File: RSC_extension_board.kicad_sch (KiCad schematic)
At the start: 23 parts, among them J1 Conn_01x03, J2 Conn_01x03, J3 Conn_01x03, J4 Raspberry_Pi_4, J5 Conn_01x04, J6 USB_C_Receptacle_PowerOnly_6P, J7 Conn_01x02, Q1 BSS138, U1 USBLC6-2SC6

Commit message: some external power stuff
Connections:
- net +5V: now also D3.3, U1.5 (VBUS)
- net Earth: now also D3.1, D3.2, U1.2 (GND)
- net at R3.1: now also U1.4 (I/O2); no longer J6.B5 (CC2)
- net at R4.1: now also U1.6 (I/O1); no longer J6.A5 (CC1)
- net at U1.1 (I/O1): now also J6.A5 (CC1)
- net at U1.3 (I/O2): now also J6.B5 (CC2)
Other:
- note added: "right now power. maybe later battery things?"
- note removed: "battery things"
- moved on the sheet: D3, R3, R4, U1

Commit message: bit of power circuit
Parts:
- added C5: 100nF, Capacitor_SMD:C_0603_1608Metric_Pad1.08x0.95mm_HandSolder, symbol Device:C
- added F1: SMDC300F_24-2, SMDC300F_24-2:SMDC030F2, symbol SMDC300F_24-2:SMDC300F_24-2
- added SW1: SW_Wuerth_450301014042, Button_Switch_THT:SW_Slide-03_Wuerth-WS-SLTV_10x2.5x6.4_P2.54mm, symbol Switch:SW_Wuerth_450301014042
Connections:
- net +5V: now also C5.2, SW1.2 (C); no longer D3.3, J6.A9 (VBUS), J6.B9 (VBUS), U1.5 (VBUS)
- net Earth: now also C5.1
- new net: F1.2, SW1.1 (B)
- new net: D3.3, F1.1, J6.A9 (VBUS), J6.B9 (VBUS), U1.5 (VBUS)
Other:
- moved on the sheet: D3

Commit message: updated fuse
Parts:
- removed F1: SMDC300F_24-2, SMDC300F_24-2:SMDC030F2, symbol SMDC300F_24-2:SMDC300F_24-2
- added F?: PTSLR08058V350, FUSC2516X100N, symbol PTSLR08058V350:PTSLR08058V350
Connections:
- net at SW1.1 (B): now also F?.2
- net at D3.3, J6.A9 (VBUS), J6.B9 (VBUS)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: now also F?.1
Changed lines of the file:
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@@
-	)
-	(symbol
-		(lib_id "SMDC300F_24-2:SMDC300F_24-2")
-		(at 52.07 151.13 0)
-		(unit 1)
-		(exclude_from_sim no)
-		(in_bom yes)
-		(on_board yes)
-		(dnp no)
-		(fields_autoplaced yes)
-		(property "Reference" "F1"
-			(at 60.96 143.51 0)
-			(effects
-				(font
-					(size 1.27 1.27)
-				)
-			)
-		)
-		(property "Value" "SMDC300F_24-2"
-			(at 60.96 146.05 0)
-			(effects
-				(font
-					(size 1.27 1.27)
-				)
-			)
-		)
-		(property "Footprint" "SMDC300F_24-2:SMDC030F2"
-			(at 66.04 247.32 0)
-			(effects
-				(font
-					(size 1.27 1.27)
-				)
-				(justify left top)
-				(hide yes)
-			)
-		)
-		(property "Datasheet" "https://www.littelfuse.com/~/media/electronics/product_specifications/resettable_ptcs/littelfuse_ptc_smdc030f_2_product_specification.pdf.pdf"
-			(at 66.04 347.32 0)
-			(effects
-				(font
-					(size 1.27 1.27)
-				)
-				(justify left top)
-				(hide yes)
-			)
-		)
-		(property "Description" "Resettable Fuses - PPTC 24V    3A-HD  40A MAX"
-			(at 52.07 151.13 0)
-			(effects
-				(font
-					(size 1.27 1.27)
-				)
-				(hide yes)
-			)
-		)
-		(property "Height" "1"
-			(at 66.04 547.32 0)
-			(effects
-				(font
-					(size 1.27 1.27)
-				)
-				(justify left top)
-				(hide yes)
-			)
-		)
-		(property "Manufacturer_Name" "LITTELFUSE"
-			(at 66.04 647.32 0)
-			(effects
-				(font
-					(size 1.27 1.27)
-				)
-				(justify left top)
-				(hide yes)
-			)
-		)
-		(property "Manufacturer_Part_Number" "SMDC300F/24-2"
-			(at 66.04 747.32 0)
-			(effects
-				(font
-					(size 1.27 1.27)
-				)
-				(justify left top)
-				(hide yes)
-			)
-		)
-		(property "Mouser Part Number" "650-SMDC300F/24-2"
-			(at 66.04 847.32 0)
-			(effects
-				(font
-					(size 1.27 1.27)
-				)
-				(justify left top)
-				(hide yes)
-			)
-		)
-		(property "Mouser Price/Stock" "https://www.mouser.co.uk/ProductDetail/Littelfuse/SMDC300F-24-2?qs=pBN%2FbMTRZdcsk20bJLIO5A%3D%3D"
-			(at 66.04 947.32 0)
-			(effects
-				(font
-					(size 1.27 1.27)
-				)
-				(justify left top)
-				(hide yes)
-			)
-		)
-		(property "Arrow Part Number" "SMDC300F/24-2"
-			(at 66.04 1047.32 0)
-			(effects
-				(font
-					(size 1.27 1.27)
-				)
-				(justify left top)
-				(hide yes)
-			)
-		)
-		(property "Arrow Price/Stock" "https://www.arrow.com/en/products/smdc300f24-2/littelfuse?utm_currency=USD&region=nac"
-			(at 66.04 1147.32 0)
-			(effects
-				(font
-					(size 1.27 1.27)
-				)
-				(justify left top)
-				(hide yes)
-			)
-		)
-		(pin "2"
-		)
-		(pin "1"
-		)
-		(instances
-			(project ""
-				(path "/1f48ed4c-84ce-4e77-88fc-25bf92dcee2d"
-					(reference "F1")
-					(unit 1)
-				)
-			)
-		)
 	)
 	(symbol
@@
 					(unit 1)
 				)
+			)
+		)
+	)
+	(symbol
+		(lib_id "PTSLR08058V350:PTSLR08058V350")
+		(at 50.8 139.7 0)
+		(unit 1)
+		(exclude_from_sim no)
+		(in_bom yes)
+		(on_board yes)
+		(dnp no)
+		(fields_autoplaced yes)
+		(property "Reference" "F?"
+			(at 57.15 146.05 0)
+			(effects
+				(font
+					(size 1.27 1.27)
+				)
+				(justify left)
+			)
+		)
+		(property "Value" "PTSLR08058V350"
+			(at 57.15 148.082 0)
+			(effects
+				(font
+					(size 1.27 1.27)
+				)
+				(justify left)
+			)
+		)
+		(property "Footprint" "FUSC2516X100N"
+			(at 67.31 234.62 0)
+			(effects
+				(font
+					(size 1.27 1.27)
+				)
+				(justify left top)
+				(hide yes)
+			)
+		)
+		(property "Datasheet" "https://www.eaton.com/content/dam/eaton/products/electronic-components/resources/data-sheet/eaton-ptslr0805-surface-mount-resettable-fuse-data-sheet.pdf"
+			(at 67.31 334.62 0)
+			(effects
+				(font
+					(size 1.27 1.27)
+				)
+				(justify left top)
+				(hide yes)
+			)
+		)
+		(property "Description" "PTSLR 0805 3.5A"
+			(at 61.214 154.432 0)
+			(effects
+				(font
+					(size 1.27 1.27)
+				)
+				(hide yes)
+			)
+		)
+		(property "Height" "1"
+			(at 67.31 534.62 0)
+			(effects
+				(font
+					(size 1.27 1.27)
+				)
+				(justify left top)
+				(hide yes)
+			)
+		)
+		(property "Manufacturer_Name" "Eaton"
+			(at 67.31 634.62 0)
+			(effects
+				(font
+					(size 1.27 1.27)
+				)
+				(justify left top)
+				(hide yes)
+			)
+		)
+		(property "Manufacturer_Part_Number" "PTSLR08058V350"
+			(at 67.31 734.62 0)
+			(effects
+				(font
+					(size 1.27 1.27)
+				)
+				(justify left top)
+				(hide yes)
+			)
+		)
+		(property "Mouser Part Number" ""
+			(at 67.31 834.62 0)
+			(effects
+				(font
+					(size 1.27 1.27)
+				)
+				(justify left top)
+				(hide yes)
+			)
+		)
+		(property "Mouser Price/Stock" ""
+			(at 67.31 934.62 0)
+			(effects
+				(font
+					(size 1.27 1.27)
+				)
+				(justify left top)
+				(hide yes)
+			)
+		)
+		(property "Arrow Part Number" ""
+			(at 67.31 1034.62 0)
+			(effects
+				(font
+					(size 1.27 1.27)
+				)
+				(justify left top)
+				(hide yes)
+			)
+		)
+		(property "Arrow Price/Stock" ""
+			(at 67.31 1134.62 0)
+			(effects
+				(font
+					(size 1.27 1.27)
+				)
+				(justify left top)
+				(hide yes)
+			)
+		)
+		(pin "1"
+		)
+		(pin "2"
+		)
+		(instances
+			(project ""
+				(path "/1f48ed4c-84ce-4e77-88fc-25bf92dcee2d"
+					(reference "F?")
+					(unit 1)
+				)

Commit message: save
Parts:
- gave numbers to parts that had none: 1
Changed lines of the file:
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@@
 		(dnp no)
 		(fields_autoplaced yes)
-		(property "Reference" "F?"
+		(property "Reference" "F1"
 			(at 57.15 146.05 0)
 			(effects
@@
 			(project ""
 				(path "/1f48ed4c-84ce-4e77-88fc-25bf92dcee2d"
-					(reference "F?")
+					(reference "F1")
 					(unit 1)
 				)

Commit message: qwiic connector and 3.3v led out
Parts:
- added C7: 100nF, Capacitor_SMD:C_0603_1608Metric_Pad1.08x0.95mm_HandSolder, symbol Device:C
- added G1: qwiic_Logo, symbol SparkFun-Qwiic:qwiic_Logo
- added J8: Conn_01x03, Connector_PinHeader_2.54mm:PinHeader_1x03_P2.54mm_Horizontal, symbol Connector_Generic:Conn_01x03
- added J9: PRT-14417, PRT-14417:SPARKFUN_PRT-14417, symbol PRT-14417:PRT-14417
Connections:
- net +3.3V: now also C7.1, J8.1 (Pin_1), J9.2
- net Earth: now also C7.2, J8.3 (Pin_3), J9.1
- net LED_3.3V: now also J8.2 (Pin_2)
- net SDA: now reaches J4.3 (SDA_I2C1/GPIO02)
- net SDA: now also J9.3
- net SCL: now reaches J4.5 (SCL_I2C1/GPIO03)
- net SCL: now also J9.4

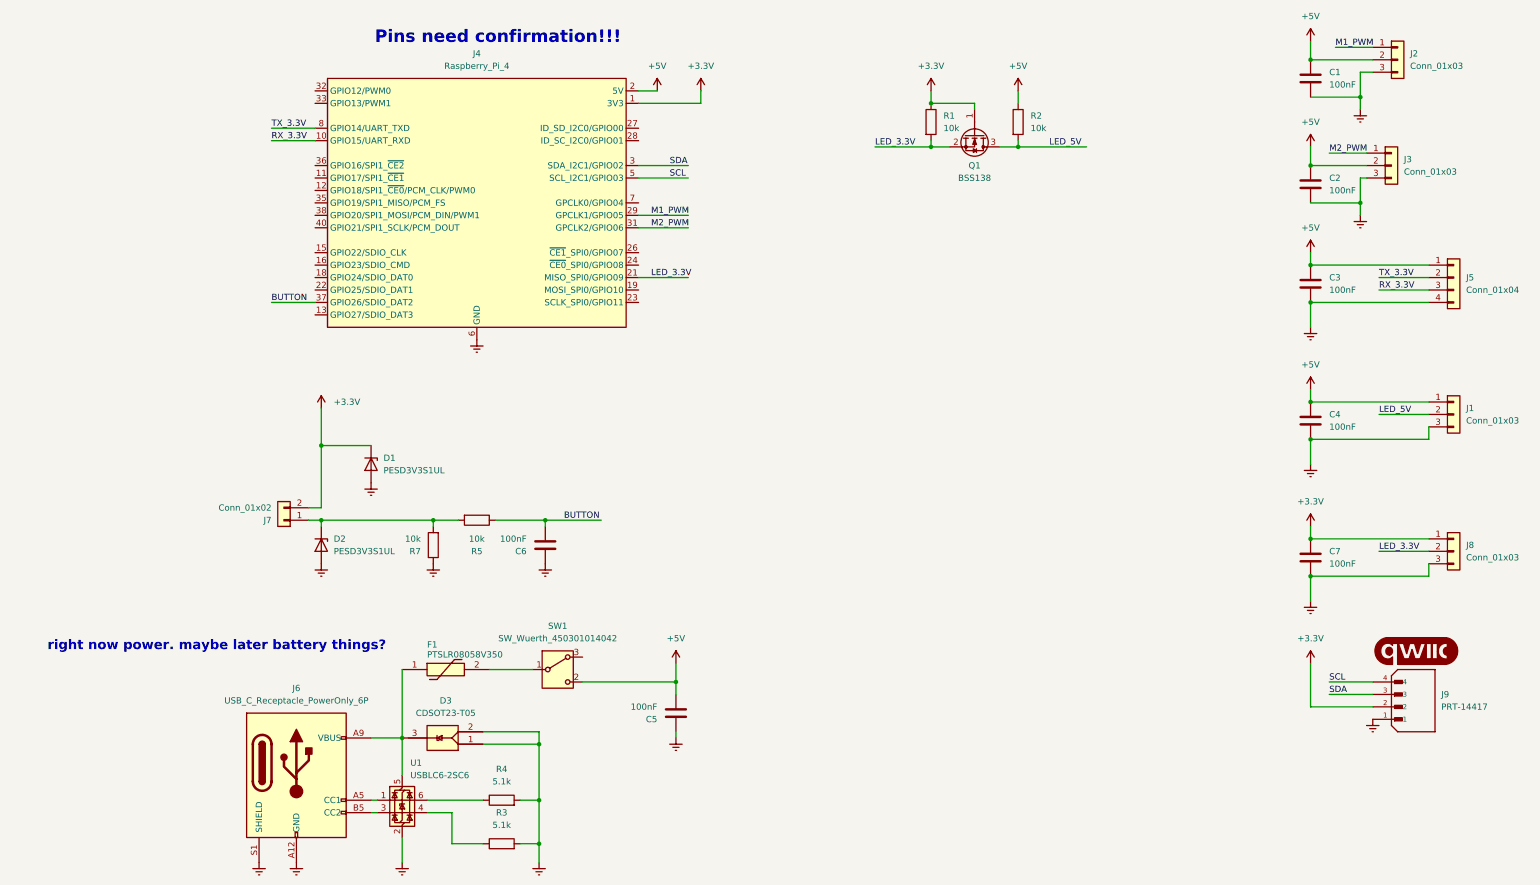
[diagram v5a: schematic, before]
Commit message: new tvs diodes
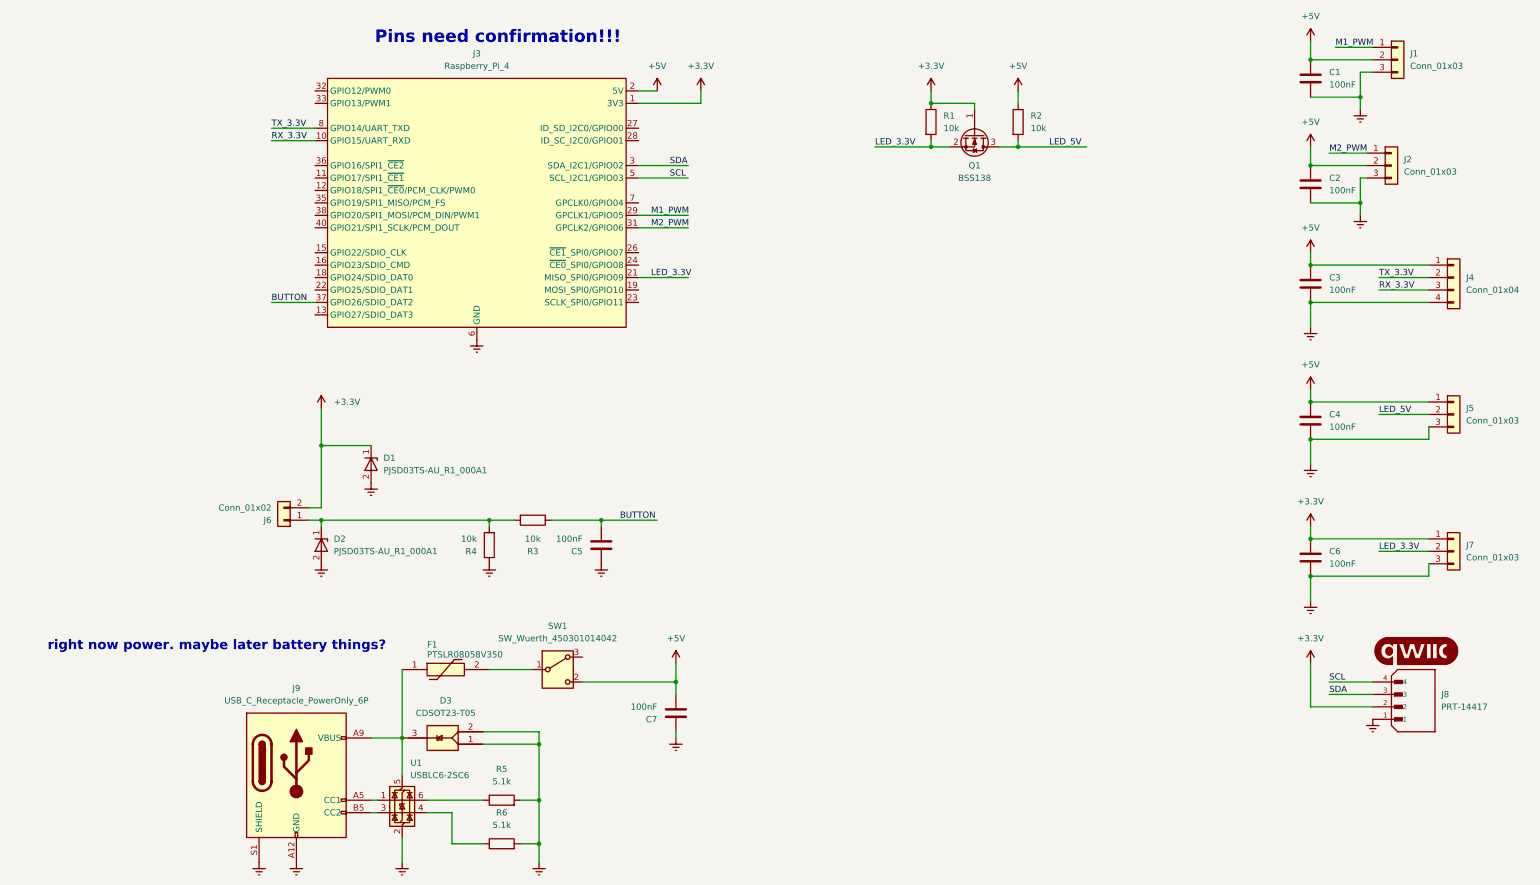
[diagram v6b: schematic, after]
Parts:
- removed D1, D2: PESD3V3S1UL, Diode_SMD:D_SOD-882, symbol Diode:PESD3V3S1UL
- added D1, D2: PJSD03TS-AU_R1_000A1, SODFL1608X65N, symbol PJSD03TS-AU_R1_000A1:PJSD03TS-AU_R1_000A1
- renumbered C6 to C5, C7 to C6, C5 to C7, J2 to J1, J3 to J2, J4 to J3, J5 to J4, J1 to J5, J7 to J6, J8 to J7, J9 to J8, J6 to J9, R5 to R3, R7 to R4, R4 to R5, R3 to R6
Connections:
- net +3.3V: now also D1.1 (K)
- net Earth: now also D1.2 (A), D2.2 (A)
- net at J6.1 (Pin_1), R3.2, R4.2: now also D2.1 (K)
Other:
- moved on the sheet: C5, R3, R4

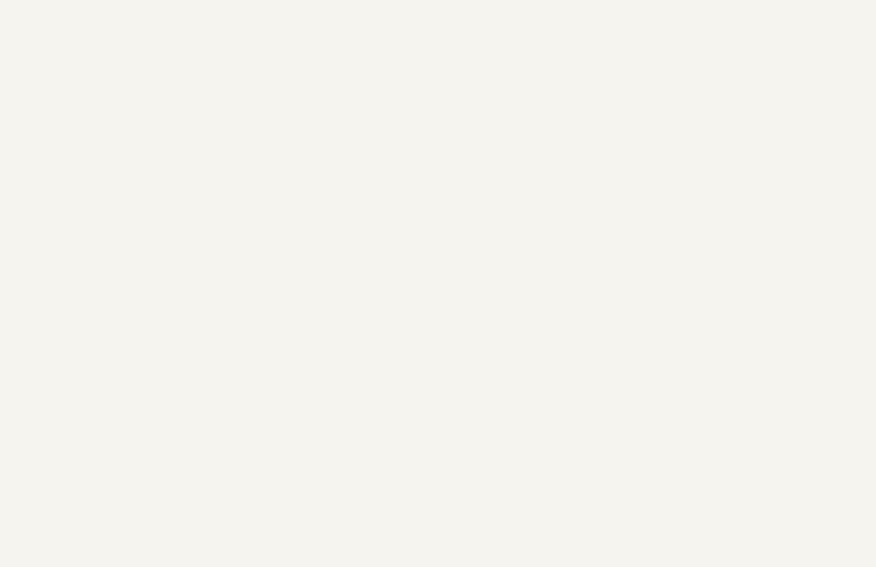
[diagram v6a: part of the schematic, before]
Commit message: added power LED
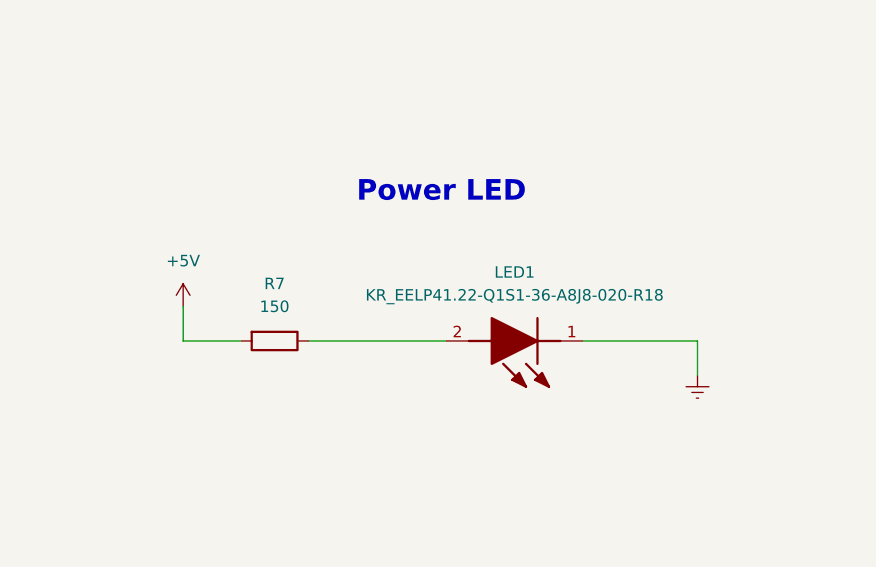
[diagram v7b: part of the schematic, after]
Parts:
- added LED1: KR_EELP41.22-Q1S1-36-A8J8-020-R18, KR_EELP41.22-Q1S1-36-A8J8-020-R18:KREELP4122Q1S136A8J8020R18, symbol KR_EELP41_22-Q1S1-36-A8J8-020-:KR_EELP41.22-Q1S1-36-A8J8-020-R18
- added R7: 150, Resistor_SMD:R_0603_1608Metric_Pad0.98x0.95mm_HandSolder, symbol Device:R
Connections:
- net +5V: now also R7.2
- net Earth: now also LED1.1 (K)
- new net: LED1.2 (A), R7.1
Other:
- note added: "Power LED"

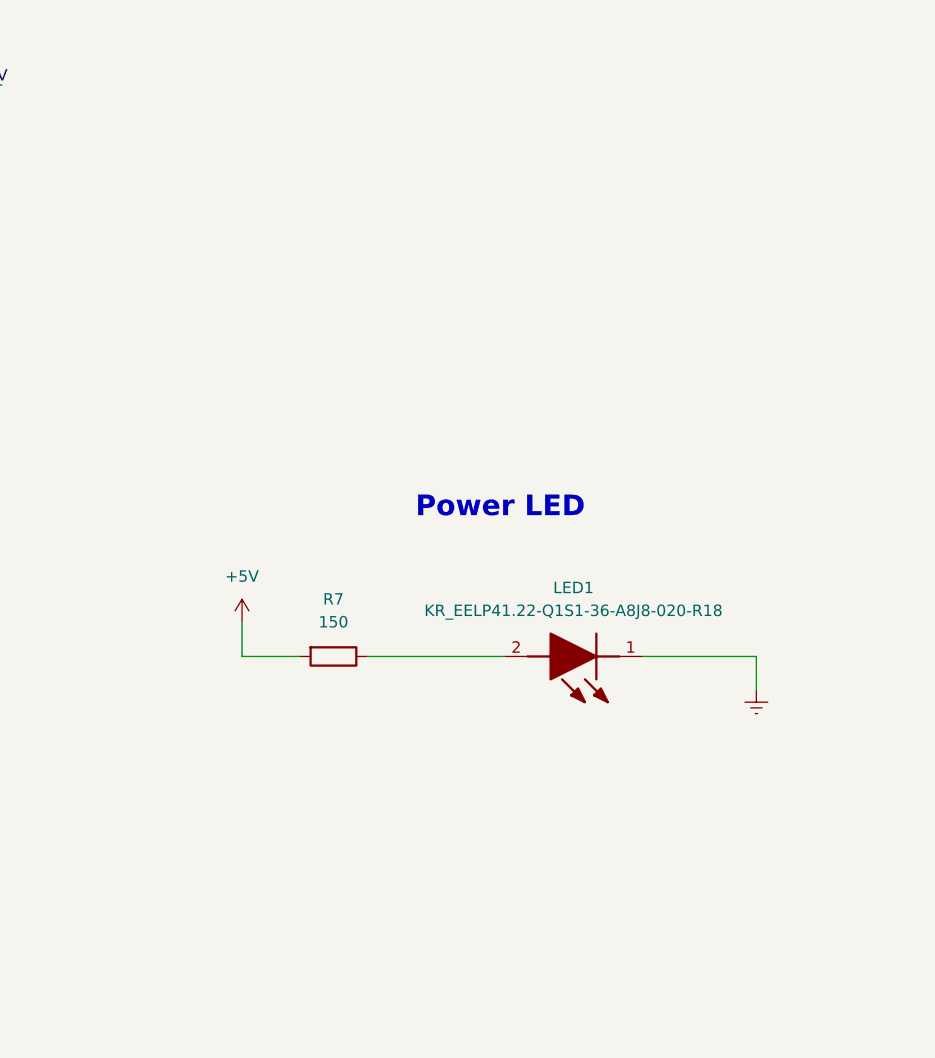
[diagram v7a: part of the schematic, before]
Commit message: added possibility for button led dimming
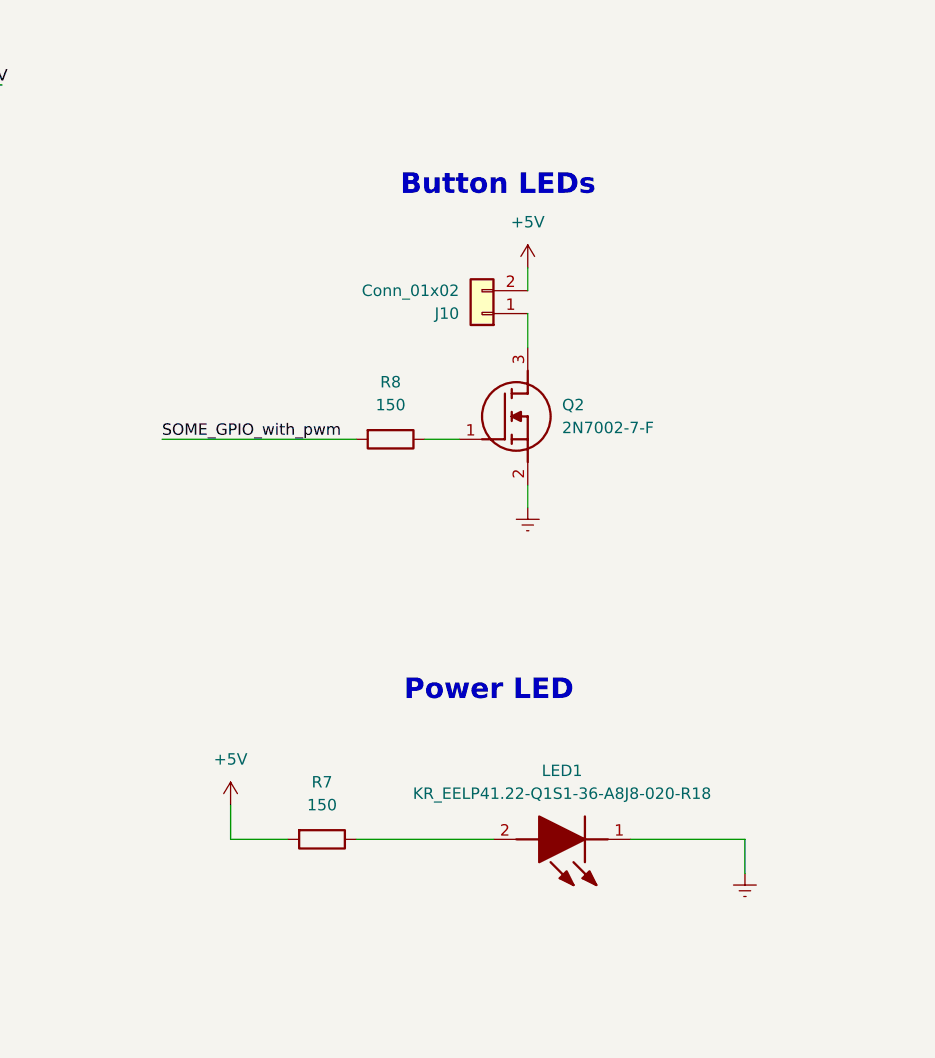
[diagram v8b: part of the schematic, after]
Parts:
- added J10: Conn_01x02, Connector_PinHeader_2.54mm:PinHeader_1x02_P2.54mm_Vertical, symbol Connector_Generic:Conn_01x02
- added Q2: 2N7002-7-F, 2N7002-7-F:SOT96P240X120-3N, symbol 2N7002-7-F:2N7002-7-F
- added R8: 150, Resistor_SMD:R_0603_1608Metric_Pad0.98x0.95mm_HandSolder, symbol Device:R
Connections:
- net +5V: now also J10.2 (Pin_2)
- net Earth: now also Q2.2 (S)
- new net: J10.1 (Pin_1), Q2.3 (D)
- new net: Q2.1 (G), R8.1
- new net SOME_GPIO_with_pwm: R8.2
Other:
- note added: "Button LEDs"
- moved on the sheet: LED1, R7
